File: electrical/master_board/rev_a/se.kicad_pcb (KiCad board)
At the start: 2 copper layers, 66.2 x 45.2 mm, 7 parts, among them CN107 BRIDGE_SE_OUTER;M1x8

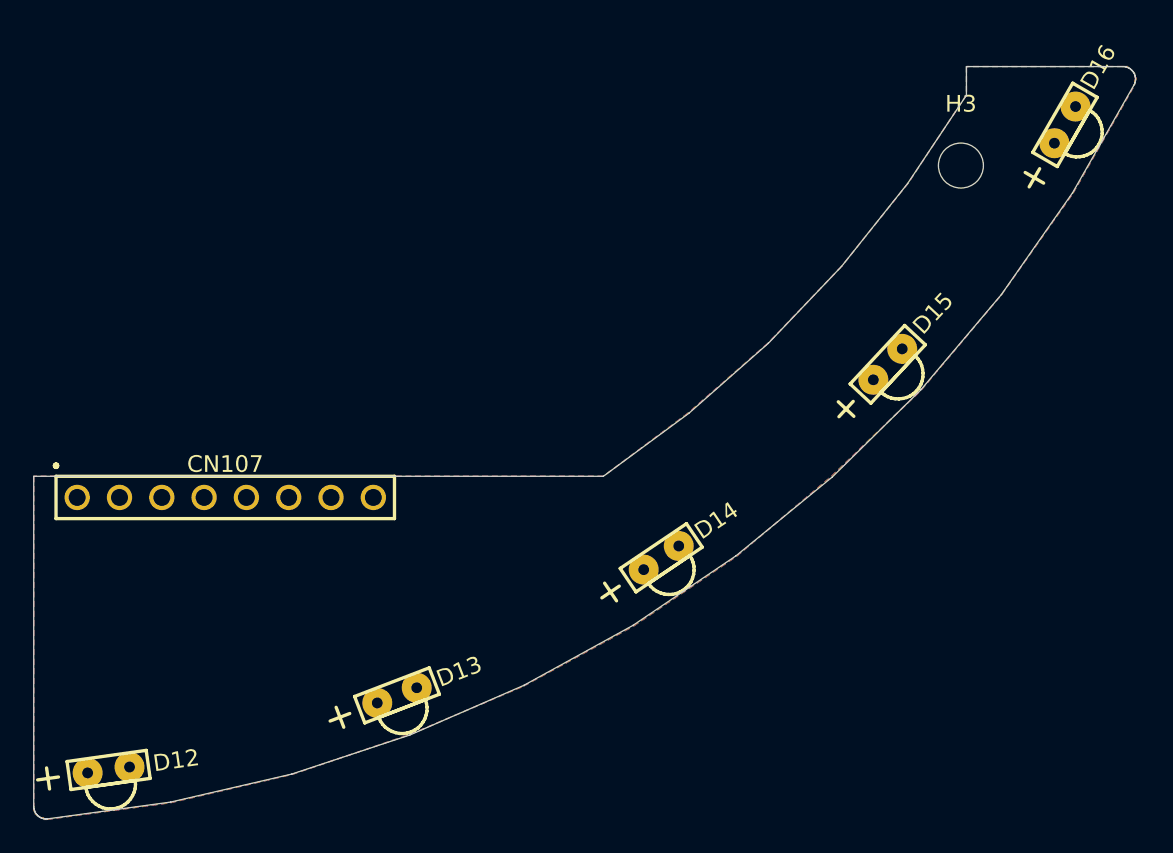
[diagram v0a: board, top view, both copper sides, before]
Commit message: Positioned all of the parts on SW board.
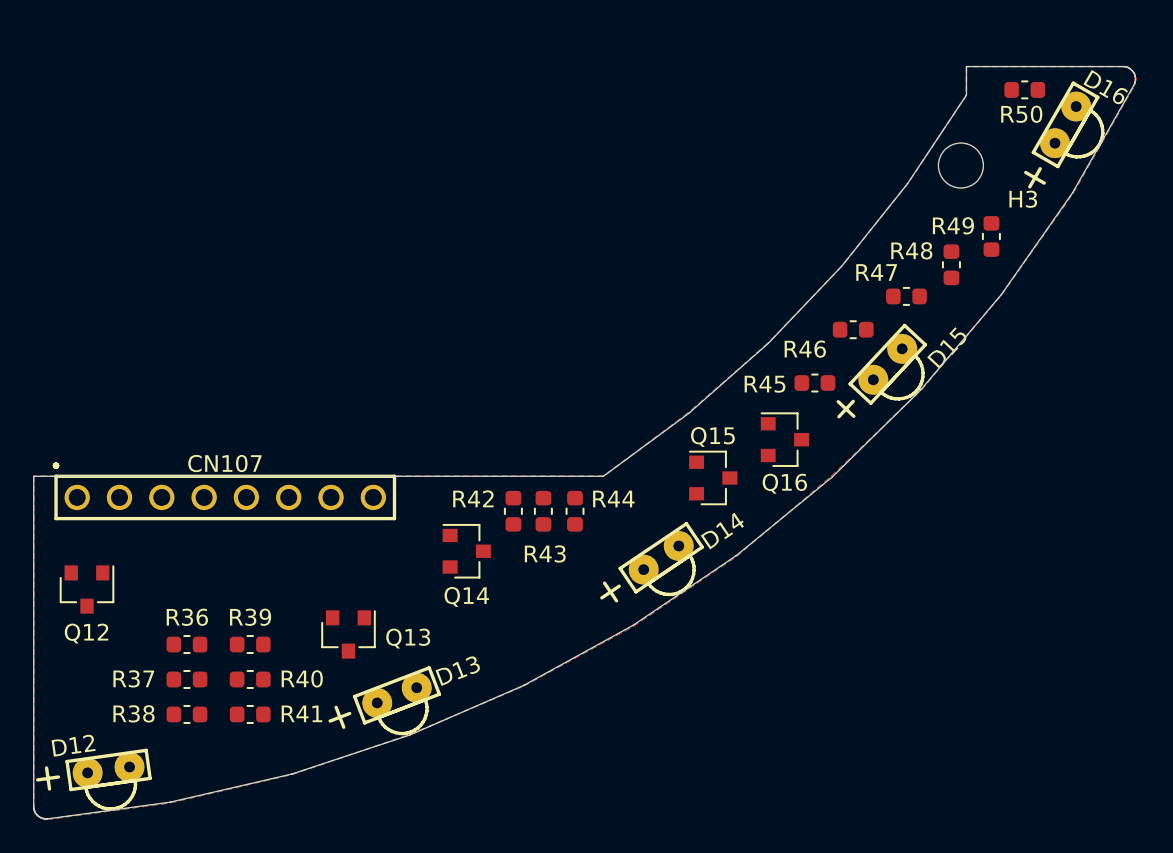
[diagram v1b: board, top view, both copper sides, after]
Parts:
- added Q12: 2N7000;SOT23, Package_TO_SOT_SMD:SOT-23, F.Cu at (109.7, 167.4)
- added Q13: 2N7000;SOT23, Package_TO_SOT_SMD:SOT-23, F.Cu at (125.4, 170.1)
- added Q14: 2N7000;SOT23, Package_TO_SOT_SMD:SOT-23, F.Cu at (132.5, 165.1)
- added Q15: 2N7000;SOT23, Package_TO_SOT_SMD:SOT-23, F.Cu at (147.3, 160.7)
- added Q16: 2N7000;SOT23, Package_TO_SOT_SMD:SOT-23, F.Cu at (151.6, 158.4)
- added R36: 330;1608, Resistor_SMD:R_0603_1608Metric, F.Cu at (115.7, 170.7)
- added R37: 330;1608, Resistor_SMD:R_0603_1608Metric, F.Cu at (115.7, 172.8)
- added R38: 330;1608, Resistor_SMD:R_0603_1608Metric, F.Cu at (115.7, 174.9)
- added R39: 330;1608, Resistor_SMD:R_0603_1608Metric, F.Cu at (119.5, 170.7)
- added R40: 330;1608, Resistor_SMD:R_0603_1608Metric, F.Cu at (119.5, 172.8)
- added R41: 330;1608, Resistor_SMD:R_0603_1608Metric, F.Cu at (119.5, 174.9)
- added R42: 330;1608, Resistor_SMD:R_0603_1608Metric, F.Cu at (135.3, 162.7)
- added R43: 330;1608, Resistor_SMD:R_0603_1608Metric, F.Cu at (137.1, 162.7)
- added R44: 330;1608, Resistor_SMD:R_0603_1608Metric, F.Cu at (139.0, 162.7)
- added R45: 330;1608, Resistor_SMD:R_0603_1608Metric, F.Cu at (153.4, 155.0)
- added R46: 330;1608, Resistor_SMD:R_0603_1608Metric, F.Cu at (155.7, 151.8)
- added R47: 330;1608, Resistor_SMD:R_0603_1608Metric, F.Cu at (158.9, 149.8)
- added R48: 330;1608, Resistor_SMD:R_0603_1608Metric, F.Cu at (161.6, 147.9)
- added R49: 330;1608, Resistor_SMD:R_0603_1608Metric, F.Cu at (164.0, 146.2)
- added R50: 330;1608, Resistor_SMD:R_0603_1608Metric, F.Cu at (166.0, 137.4)
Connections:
- CN107 pad 1: /GND -> Net-(CN107-Pad1)
- CN107 pad 2: Net-(CN107-Pad2) -> /9V
- CN107 pad 3: Net-(CN107-Pad3) -> /LED12
- CN107 pad 4: Net-(CN107-Pad4) -> /LED13
- CN107 pad 5: Net-(CN107-Pad5) -> /LED14
- CN107 pad 6: Net-(CN107-Pad6) -> /LED15
- CN107 pad 7: Net-(CN107-Pad7) -> /LED16
- CN107 pad 8: Net-(CN107-Pad8) -> /GND

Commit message: Did initial SE board layout. Passes DRC.
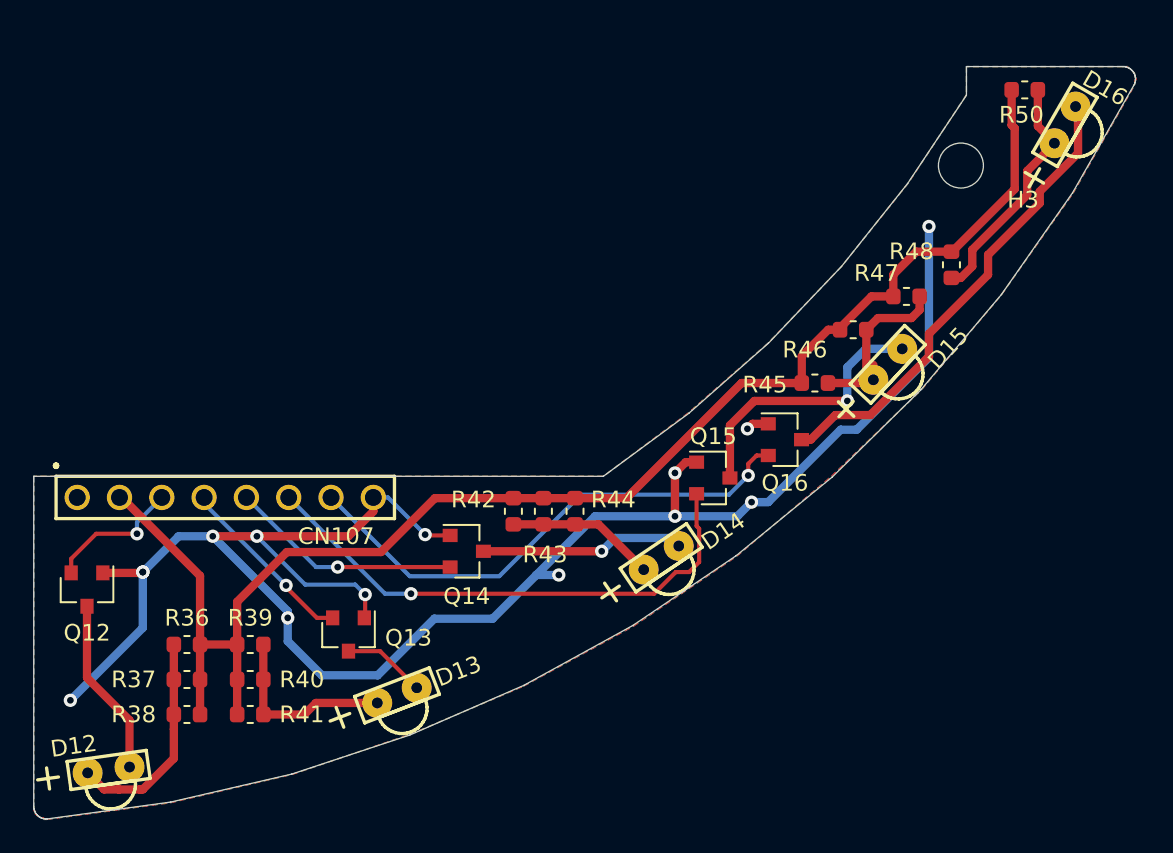
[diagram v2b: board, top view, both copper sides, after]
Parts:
- removed R49: 330;1608, Resistor_SMD:R_0603_1608Metric
- turned R40 to 180 degrees
- turned R41 to 180 degrees
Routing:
- net /GND: track 0.00 -> 113.2 mm, vias 0 -> 14
- net /9V: track 0.00 -> 88.9 mm
- net /LED15: track 0.00 -> 32.0 mm, vias 0 -> 1
- net /LED16: track 0.00 -> 31.6 mm, vias 0 -> 1
- net Net-(D16-Pad1): track 0.00 -> 28.5 mm
- net Net-(D15-Pad1): track 0.00 -> 16.6 mm, vias 0 -> 1
- net Net-(D16-Pad2): track 0.00 -> 14.7 mm
- net /LED14: track 0.00 -> 14.0 mm, vias 0 -> 1
- net Net-(D12-Pad2): track 0.00 -> 13.2 mm
- net Net-(D14-Pad1): track 0.00 -> 12.3 mm, vias 0 -> 1
- net Net-(D15-Pad2): track 0.00 -> 11.4 mm
- net Net-(D13-Pad2): track 0.00 -> 11.3 mm
- net /LED13: track 0.00 -> 11.0 mm, vias 0 -> 1
- net Net-(D12-Pad1): track 0.00 -> 10.7 mm
- net Net-(D14-Pad2): track 0.00 -> 8.95 mm
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
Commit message: Got NE PCB done.
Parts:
- added R49: 330Ω;1608, Resistor_SMD:R_0603_1608Metric, F.Cu at (164.0, 146.2)
- R36, R37, R38, R39, R40, R41, R42, R43, R44, R45, R46, R47, R48, R50: value 330;1608 -> 330Ω;1608
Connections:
- CN107 pad 1: Net-(CN107-Pad1) -> /GND
- CN107 pad 8: /GND -> Net-(CN107-Pad8)
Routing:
- net /GND: track 113.2 -> 115.5 mm, vias 14 -> 16
- net /9V: track 88.9 -> 89.5 mm
